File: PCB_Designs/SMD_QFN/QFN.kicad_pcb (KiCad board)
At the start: 2 copper layers, 40.6 x 17.7 mm, 12 parts, among them J1 USB-AM-S-X-X-TH, U1 ATtiny85-20M, Y1 12MHz

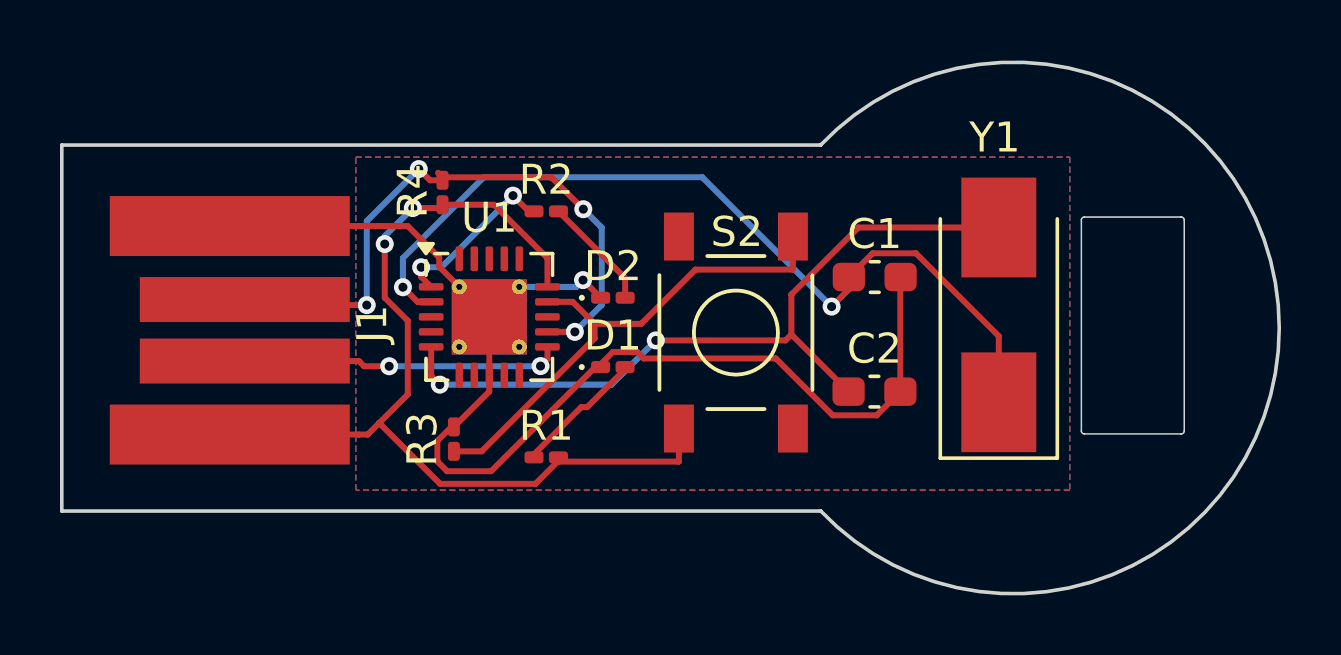
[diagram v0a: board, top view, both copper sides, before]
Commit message: Reposition LEDs on PCB for 3D enclosure alignment
Moved LEDs to new positions on the PCB to ensure proper fit and alignment with the 3D enclosure design. This adjustment accommodates the enclosure's dimensions and improves overall integration.
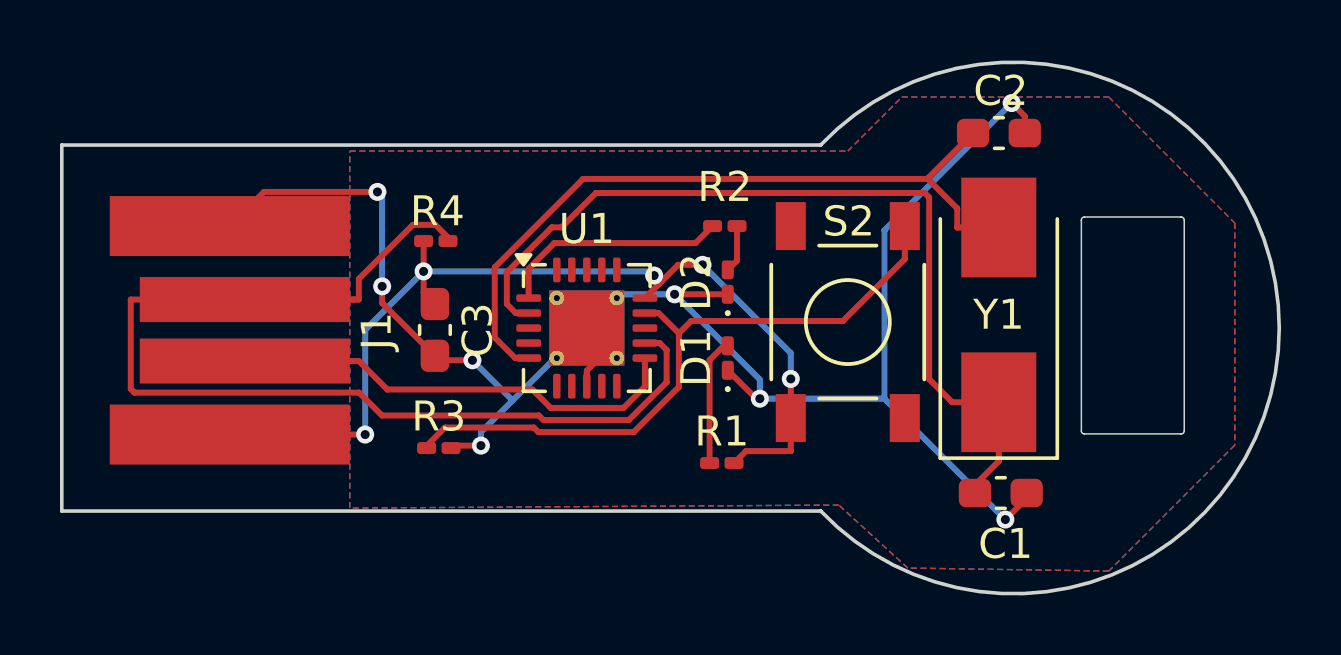
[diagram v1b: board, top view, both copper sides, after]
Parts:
- added C3: 0.1uF, Capacitor_SMD:C_0603_1608Metric_Pad1.08x0.95mm_HandSolder, F.Cu at (150.8, 83.7)
- moved C2 9.57 mm to (169.6, 77.1)
- moved C1 8.34 mm to (169.7, 89.1)
- moved R2 5.97 mm to (160.5, 80.2)
- moved R1 5.86 mm to (160.4, 88.1)
- moved D2 3.87 mm to (160.6, 82.1), turned to 90 degrees
- moved D1 3.84 mm to (160.6, 84.6), turned to 90 degrees
- moved S2 3.75 mm to (164.6, 83.4)
- moved U1 3.27 mm to (155.9, 83.6)
- moved R4 1.63 mm to (150.9, 80.7), turned to 0 degrees
- moved R3 0.58 mm to (151.0, 87.6), turned to 0 degrees
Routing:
- net GND: track 45.8 -> 62.2 mm, vias 1 -> 8
- net /Data+: track 21.4 -> 36.0 mm, vias 4 -> 0
- net Net-(U1-PB2): track 17.1 -> 22.3 mm
- net /Data-: track 10.7 -> 15.2 mm, vias 2 -> 0
- net Net-(D2-A): track 3.80 -> 1.59 mm
- net Net-(U1-~{RESET}/PB5): track 5.76 -> 7.70 mm, vias 2 -> 0
- net +5V: track 32.0 -> 32.9 mm, vias 2 -> 5
- net Net-(U1-XTAL2/PB4): track 25.7 -> 25.0 mm, vias 2 -> 0
- net Net-(U1-XTAL1/PB3): vias 2 -> 0
- added copper zone on B.Cu, net +5V
- added copper zone on F.Cu, net GND
- removed copper zone on F.Cu, net +5V
- removed copper zone on B.Cu, net GND
